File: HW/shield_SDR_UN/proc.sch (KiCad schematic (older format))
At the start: 53 parts

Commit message: bus-v2 proc-fpga
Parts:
- removed R? (x15): 39, symbol Device:R
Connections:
- net +5V is gone; now on net 3V3 MCU: J?.19 (Pin_19)
- net ADD_DAT_15 is gone; now on net GPIO_MCU_1: U?.10 ((PF0)(I2C2_SDA)(FMC_A0)(EVENTOUT))
- net ADD_DAT_16 is gone; now on net GPIO_MCU_2: U?.11 ((PF1)(I2C2_SCL)(FMC_A1)(EVENTOUT))
- net ADD_DAT_17 is gone; now on net GPIO_MCU_3: U?.12 ((PF2)(I2C2_SMBA)(FMC_A2)(EVENTOUT))
- net ADD_DAT_18 is gone; now on net GPIO_MCU_4: U?.13 ((PF3)(FMC_A3)(EVENTOUT)(ADC3_IN9))
- net ADD_DAT_19 is gone; now on net GPIO_MCU_5: U?.14 ((PF4)(FMC_A4)(EVENTOUT)(ADC3_IN14))
- net ADD_DAT_20 is gone; now on net GPIO_MCU_6: U?.15 ((PF5)(FMC_A5)(EVENTOUT)(ADC3_IN15))
- net ADD_DAT_21 is gone; now on net GPIO_MCU_7: U?.18 ((PF6)(TIM10_CH1)(SPI5_NSS)(SAI1_SD_B)(UART7_RX)(QUADSPI_BK1_IO3)(EVENTOUT)(ADC3_IN4))
- net ADD_DAT_22 is gone; now on net GPIO_MCU_8: U?.19 ((PF7)(TIM11_CH1)(SPI5_SCK)(SAI1_MCLK_B)(UART7_TX)(QUADSPI_BK1_IO2)(EVENTOUT)(ADC3_IN5))
- net ADD_DAT_23 is gone; now on net GPIO_MCU_9: U?.20 ((PF8)(SPI5_MISO)(SAI1_SCK_B)(UART7_RTS)(TIM13_CH1)(QUADSPI_BK1_IO0)(EVENTOUT)(ADC3_IN6))
- net ADD_DAT_24 is gone; now on net GPIO_MCU_10: U?.21 ((PF9)(SPI5_MOSI)(SAI1_FS_B)(UART7_CTS)(TIM14_CH1)(QUADSPI_BK1_IO1)(EVENTOUT)(ADC3_IN7))
- net ADD_DAT_25 is gone; now on net GPIO_MCU_11: U?.22 ((PF10)(EVENTOUT)(ADC3_IN8))
- net GPIO_MCU_1: no longer U?.141 ((PE0)(TIM4_ETR)(LPTIM1_ETR)(UART8_Rx)(SAI2_MCK_A)(FMC_NBL0)(EVENTOUT))
- net GPIO_MCU_10: no longer U?.60 ((PE9)(TIM1_CH1)(UART7_RTS)(QUADSPI_BK2_IO2)(FMC_D6)(EVENTOUT))
- net GPIO_MCU_11: no longer U?.63 ((PE10)(TIM1_CH2N)(UART7_CTS)(QUADSPI_BK2_IO3)(FMC_D7)(EVENTOUT))
- net GPIO_MCU_12: now also U?.26 ((SAI2_FS_B)(OTG_HS_ULPI_STP)(FMC_SDNWE)(EVENTOUT)(ADC1_IN10)(ADC2_IN10)(ADC3_IN10)(PC0)); no longer U?.64 ((PE11)(TIM1_CH2)(SPI4_NSS)(SAI2_SD_B)(FMC_D8)(EVENTOUT))
- net GPIO_MCU_13: now also U?.27 ((TRACED0)(SPI2_MOSI/I2S2_SD)(SAI1_SD_A)(EVENTOUT)(ADC1_IN11)(ADC2_IN11)(ADC3_IN11)(RTC_TAMP3)(WKUP3)(PC1)); no longer U?.65 ((PE12)(TIM1_CH3N)(SPI4_SCK)(SAI2_SCK_B)(FMC_D9)(EVENTOUT))
- net GPIO_MCU_14: now also U?.28 ((SPI2_MISO)(OTG_HS_ULPI_DIR)(FMC_SDNE0)(EVENTOUT)(ADC1_IN12)(ADC2_IN12)(ADC3_IN12)(PC2)); no longer U?.66 ((PE13)(TIM1_CH3)(SPI4_MISO)(SAI2_FS_B)(FMC_D10)(EVENTOUT))
- net GPIO_MCU_15: now also U?.29 ((SPI2_MOSI/I2S2_SD)(OTG_HS_ULPI_NXT)(FMC_SDCKE0)(EVENTOUT)(ADC1_IN13)(ADC2_IN13)(ADC3_IN13)(PC3)); no longer U?.67 ((PE14)(TIM1_CH4)(SPI4_MOSI)(SAI2_MCK_B)(FMC_D11)(EVENTOUT))
- net GPIO_MCU_16: now also U?.136 ((TIM4_CH1)(I2C1_SCL)(USART1_TX)(QUAD_SPI_BK1_NCS)(FMC_SDNE1)(EVENTOUT)(PB6)); no longer U?.68 ((PE15)(TIM1_BKIN)(FMC_D12)(EVENTOUT))
- net GPIO_MCU_2: no longer U?.142 ((PE1)(LPTIM1_IN2)(UART8_Tx)(FMC_NBL1)(EVENTOUT))
- net GPIO_MCU_3: no longer U?.1 ((PE2)(TRACECLK)(SPI4_SCK)(SAI1_MCLK_A)(QUADSPI_BK1_IO2)(FMC_A23)(EVENTOUT))
- net GPIO_MCU_4: no longer U?.2 ((PE3)(TRACED0)(SAI1_SD_B)(FMC_A19)(EVENTOUT))
- net GPIO_MCU_5: no longer U?.3 ((PE4)(TRACED1)(SPI4_NSS)(SAI1_FS_A)(FMC_A20)(EVENTOUT))
- net GPIO_MCU_6: no longer U?.4 ((PE5)(TRACED2)(TIM9_CH1)(SPI4_MISO)(SAI1_SCK_A)(FMC_A21)(EVENTOUT))
- net GPIO_MCU_7: no longer U?.5 ((PE6)(TRACED3)(TIM1_BKIN2)(TIM9_CH2)(SPI4_MOSI)(SAI1_SD_A)(SAI2_MCK_B)(FMC_A22)(EVENTOUT))
- net GPIO_MCU_8: no longer U?.58 ((PE7)(TIM1_ETR)(UART7_Rx)(QUADSPI_BK2_IO0)(FMC_D4)(EVENTOUT))
- net GPIO_MCU_9: no longer U?.59 ((PE8)(TIM1_CH1N)(UART7_Tx)(QUADSPI_BK2_IO1)(FMC_D5)(EVENTOUT))
- net FMC_NL: now reaches U?.137 ((TIM4_CH2)(I2C1_SDA)(USART1_RX)(FMC_NL)(EVENTOUT)(PB7))
- net I2C1_SCL: now reaches U?.139 ((TIM4_CH3)(TIM10_CH1)(I2C1_SCL)(CAN1_RX)(SDMMC2_D4)(SDMMC1_D4)(EVENTOUT)(PB8))
- net I2C1_SDA: now reaches U?.140 ((TIM4_CH4)(TIM11_CH1)(I2C1_SDA)(SPI2_NSS/I2S2_WS)(CAN1_TX)(SDMMC2_D5)(SDMMC1_D5)(EVENTOUT)(PB9))
- net FMC_D13: now reaches U?.77 ((USART3_TX)(FMC_D13)(EVENTOUT)(PD8))
- net FMC_D14: now reaches U?.78 ((USART3_RX)(FMC_D14)(EVENTOUT)(PD9))
- net FMC_D15: now reaches U?.79 ((USART3_CK)(FMC_D15)(EVENTOUT)(PD10))
- net FMC_A16: now reaches U?.80 ((USART3_CTS)(QUADSPI_BK1_IO0)(SAI2_SD_A)(FMC_A16/FMC_CLE)(EVENTOUT)(PD11))
- net FMC_A17: now reaches U?.81 ((TIM4_CH1)(LPTIM1_IN1)(USART3_RTS)(QUADSPI_BK1_IO1)(SAI2_FS_A)(FMC_A17/FMC_ALE)(EVENTOUT)(PD12))
- net FMC_A18: now reaches U?.82 ((TIM4_CH2)(LPTIM1_OUT)(QUADSPI_BK1_IO3)(SAI2_SCK_A)(FMC_A18)(EVENTOUT)(PD13))
- net FMC_D0: now reaches U?.85 ((TIM4_CH3)(UART8_CTS)(FMC_D0)(EVENTOUT)(PD14))
- net FMC_D1: now reaches U?.86 ((TIM4_CH4)(UART8_RTS)(FMC_D1)(EVENTOUT)(PD15))
- net FMC_A14: now reaches U?.89 ((PG4)(FMC_A14/FMC_BA0)(EVENTOUT))
- net FMC_A15: now reaches U?.90 ((PG5)(FMC_A15/FMC_BA1)(EVENTOUT))
- net ADD_DAT_26: no longer names the net of U?.49 ((PF11)(SPI5_MOSI)(SAI2_SD_B)(FMC_SDNRAS)(EVENTOUT))
- net ADD_DAT_27: no longer names the net of U?.50 ((PF12)(FMC_A6)(EVENTOUT))
- net ADD_DAT_28: no longer names the net of U?.53 ((PF13)(FMC_A7)(EVENTOUT))
- net ADD_DAT_29: no longer names the net of U?.54 ((PF14)(FMC_A8)(EVENTOUT))
- net ADD_DAT_30: no longer names the net of U?.55 ((PF15)(FMC_A9)(EVENTOUT))
- net P_FPGA_1: no longer names the net of U?.113 ((TRACED3)(SPI3_MOSI/I2S3_SD)(USART3_CK)(UART5_TX)(SDMMC1_CK)(EVENTOUT)(PC12))
- net P_FPGA_10: no longer names the net of U?.124 ((USART6_RX)(QUADSPI_BK2_IO2)(SAI2_FS_B)(SDMMC2_D0)(FMC_NE2/FMC_NCE)(EVENTOUT)(PG9))
- net P_FPGA_11: no longer names the net of U?.125 ((PG10)(SAI2_SD_B)(SDMMC2_D1)(FMC_NE3)(EVENTOUT))
- net P_FPGA_12: no longer names the net of U?.126 ((PG11)(SDMMC2_D2)(FMC_INT)(EVENTOUT))
- net P_FPGA_13: no longer names the net of U?.127 ((PG12)(LPTIM1_IN1)(USART6_RTS)(SDMMC2_D3)(FMC_NE4)(EVENTOUT))
- net P_FPGA_14: no longer names the net of U?.128 ((PG13)(TRACED0)(LPTIM1_OUT)(USART6_CTS)(FMC_A24)(EVENTOUT))
- net P_FPGA_15: no longer names the net of U?.129 ((PG14)(TRACED1)(LPTIM1_ETR)(USART6_TX)(QUADSPI_BK2_IO3)(FMC_A25)(EVENTOUT))
- net P_FPGA_2 renamed FMC_D2
- net P_FPGA_3 renamed FMC_D3
- net P_FPGA_4: no longer names the net of U?.116 ((TRACED2)(TIM3_ETR)(UART5_RX)(SDMMC1_CMD)(EVENTOUT)(PD2))
- net P_FPGA_5 renamed FMC_CLK
- net P_FPGA_6 renamed FMC_NOE
- net P_FPGA_7 renamed FMC_NWE
- net P_FPGA_8 renamed FMC_NWAIT
- net P_FPGA_9 renamed FMC_NE1
- new net FMC_A19: U?.2 ((PE3)(TRACED0)(SAI1_SD_B)(FMC_A19)(EVENTOUT))
- new net FMC_A20: U?.3 ((PE4)(TRACED1)(SPI4_NSS)(SAI1_FS_A)(FMC_A20)(EVENTOUT))
- new net FMC_A21: U?.4 ((PE5)(TRACED2)(TIM9_CH1)(SPI4_MISO)(SAI1_SCK_A)(FMC_A21)(EVENTOUT))
- new net FMC_A22: U?.5 ((PE6)(TRACED3)(TIM1_BKIN2)(TIM9_CH2)(SPI4_MOSI)(SAI1_SD_A)(SAI2_MCK_B)(FMC_A22)(EVENTOUT))
- new net FMC_A23: U?.1 ((PE2)(TRACECLK)(SPI4_SCK)(SAI1_MCLK_A)(QUADSPI_BK1_IO2)(FMC_A23)(EVENTOUT))
- new net FMC_D10: U?.66 ((PE13)(TIM1_CH3)(SPI4_MISO)(SAI2_FS_B)(FMC_D10)(EVENTOUT))
- new net FMC_D11: U?.67 ((PE14)(TIM1_CH4)(SPI4_MOSI)(SAI2_MCK_B)(FMC_D11)(EVENTOUT))
- new net FMC_D12: U?.68 ((PE15)(TIM1_BKIN)(FMC_D12)(EVENTOUT))
- new net FMC_D4: U?.58 ((PE7)(TIM1_ETR)(UART7_Rx)(QUADSPI_BK2_IO0)(FMC_D4)(EVENTOUT))
- new net FMC_D5: U?.59 ((PE8)(TIM1_CH1N)(UART7_Tx)(QUADSPI_BK2_IO1)(FMC_D5)(EVENTOUT))
- new net FMC_D6: U?.60 ((PE9)(TIM1_CH1)(UART7_RTS)(QUADSPI_BK2_IO2)(FMC_D6)(EVENTOUT))
- new net FMC_D7: U?.63 ((PE10)(TIM1_CH2N)(UART7_CTS)(QUADSPI_BK2_IO3)(FMC_D7)(EVENTOUT))
- new net FMC_D8: U?.64 ((PE11)(TIM1_CH2)(SPI4_NSS)(SAI2_SD_B)(FMC_D8)(EVENTOUT))
- new net FMC_D9: U?.65 ((PE12)(TIM1_CH3N)(SPI4_SCK)(SAI2_SCK_B)(FMC_D9)(EVENTOUT))
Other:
- note added: "BUS DATA-ADDRESS-CONTROL \nPROC<->FPGA\n"
- note added: "FMC_NADV o NL\n"

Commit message: algunos footprint
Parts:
- added L? (x2): bead, 600R, 350 mA, Inductor_SMD:L_0603_1608Metric_Pad1.05x0.95mm_HandSolder, symbol Device:L
- added Y?: ABM8G-25.000MHZ-B4Y-T, UL_ABM9G25000MHZB4YT:ABM8G-25.000MHZ-B4Y-T, symbol UL_ABM9G25000MHZB4YT:ABM8G-25.000MHZ-B4Y-T
- BT?: footprint (none) -> modules:BAT-HLD-001; digikey (none) -> BAT-HLD-001-ND
- C? (x4): footprint (none) -> Capacitor_SMD:C_0603_1608Metric_Pad1.05x0.95mm_HandSolder
- D? (x2): footprint (none) -> LED_SMD:LED_0805_2012Metric_Pad1.15x1.40mm_HandSolder
- J?: footprint (none) -> Connector_PinSocket_2.54mm:PinSocket_2x20_P2.54mm_Vertical; DIGIKEY (none) -> S6106-ND
- R? (x4): footprint (none) -> Resistor_SMD:R_0603_1608Metric_Pad1.05x0.95mm_HandSolder
- U?: footprint (none) -> Package_QFP:LQFP-144_20x20mm_P0.5mm; digikey (none) -> 497-18558-ND
- X?: footprint (none) -> CRISTAL_4:GSG-XTAL3.2x2.5mm; digikey 535-10297-1-ND////535-11296-1-ND -> 535-10289-1-ND
- X?: footprint (none) -> CRISTAL_4:NX3215SA; digikey SER4103CT-ND -> 644-1171-1-ND
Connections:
- wire segments 328 -> 329
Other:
- note added: "587-1897-1-ND"

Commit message: algunos footprint_v2
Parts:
- removed X?: GSG-XTAL4PIN, CRISTAL_4:GSG-XTAL3.2x2.5mm, symbol hackrf-one-rescue:GSG-XTAL4PIN
- removed Y?: ABM8G-25.000MHZ-B4Y-T, UL_ABM9G25000MHZB4YT:ABM8G-25.000MHZ-B4Y-T, symbol UL_ABM9G25000MHZB4YT:ABM8G-25.000MHZ-B4Y-T
- added Y?e: GSG-XTAL4PIN, CRISTAL_4:GSG-XTAL3.2x2.5mm, symbol UL_ABM9G25000MHZB4YT:ABM8G-25.000MHZ-B4Y-T
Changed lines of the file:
@@
-$EndComp
-$Comp
-L hackrf-one-rescue:GSG-XTAL4PIN X?
-U 0 0 5CD3D0E7
-P 2100 4700
-F 0 "X?" H 2100 5083 60  0000 C CNN
-F 1 "GSG-XTAL4PIN" H 2100 4977 60  0000 C CNN
-F 2 "CRISTAL_4:GSG-XTAL3.2x2.5mm" H 2100 4700 60  0001 C CNN
-F 3 "" H 2100 4700 60  0000 C CNN
-F 4 "16MHz - 10pF" H 2100 4879 50  0000 C CNN "frecuencia"
-F 5 "	535-10289-1-ND" H 2100 4700 50  0001 C CNN "digikey"
-	0    2100 4700
-	1    0    0    -1
 $EndComp
 $Comp
 L power:GND #PWR0164
 U 1 1 5CD657FB
-P 2000 5100
-F 0 "#PWR0164" H 2000 4850 50  0001 C CNN
-F 1 "GND" H 2005 4927 50  0000 C CNN
-F 2 "" H 2000 5100 50  0001 C CNN
-F 3 "" H 2000 5100 50  0001 C CNN
-	1    2000 5100
-	1    0    0    -1
+P 2050 4500
+F 0 "#PWR0164" H 2050 4250 50  0001 C CNN
+F 1 "GND" H 2055 4327 50  0000 C CNN
+F 2 "" H 2050 4500 50  0001 C CNN
+F 3 "" H 2050 4500 50  0001 C CNN
+	1    2050 4500
+	0    1    1    0
 $EndComp
 $Comp
 L power:GND #PWR0165
 U 1 1 5CD65D12
-P 2200 5100
-F 0 "#PWR0165" H 2200 4850 50  0001 C CNN
-F 1 "GND" H 2205 4927 50  0000 C CNN
-F 2 "" H 2200 5100 50  0001 C CNN
-F 3 "" H 2200 5100 50  0001 C CNN
-	1    2200 5100
-	1    0    0    -1
-$EndComp
-Wire Wire Line
-	2000 5100 2000 5000
-Wire Wire Line
-	2200 5100 2200 5000
+P 2150 5000
+F 0 "#PWR0165" H 2150 4750 50  0001 C CNN
+F 1 "GND" H 2155 4827 50  0000 C CNN
+F 2 "" H 2150 5000 50  0001 C CNN
+F 3 "" H 2150 5000 50  0001 C CNN
+	1    2150 5000
+	1    0    0    -1
+$EndComp
+Wire Wire Line
+	2050 4500 2150 4500
+Wire Wire Line
+	2150 5000 2150 4900
 $Comp
 L Device:C C?
@@
 Wire Wire Line
 	2750 4700 2400 4700
-Wire Wire Line
-	1800 4700 1450 4700
 Wire Wire Line
 	1450 4700 1450 4800
@@
 $Comp
 L hackrf-one-rescue:CRYSTAL X?
-U 0 0 5CDEC498
+U 1 1 5CDEC498
 P 2100 6200
 F 0 "X?" H 2100 6582 60  0000 C CNN
@@
 F 4 "32.768KHz -- 6pF" H 2100 6378 50  0000 C CNN "frecuencia"
 F 5 "644-1171-1-ND" H 2100 6200 50  0001 C CNN "digikey"
-	0    2100 6200
+	1    2100 6200
 	1    0    0    -1
 $EndComp
@@
 $Comp
 L Device:R R?
-U 0 0 5CD462E5
+U 1 1 5CD462E5
 P 1350 9800
 F 0 "R?" V 1450 9800 50  0000 L CNN
@@
 F 2 "Resistor_SMD:R_0603_1608Metric_Pad1.05x0.95mm_HandSolder" V 1280 9800 50  0001 C CNN
 F 3 "~" H 1350 9800 50  0001 C CNN
-	0    1350 9800
+	1    1350 9800
 	0    -1   -1   0
 $EndComp
@@
 $Comp
 L Device:LED D?
-U 0 0 5CE7E335
+U 1 1 5CE7E335
 P 16550 2000
 F 0 "D?" V 16589 1883 50  0000 R CNN
@@
 F 2 "LED_SMD:LED_0805_2012Metric_Pad1.15x1.40mm_HandSolder" H 16550 2000 50  0001 C CNN
 F 3 "~" H 16550 2000 50  0001 C CNN
-	0    16550 2000
+	1    16550 2000
 	0    -1   -1   0
 $EndComp
 $Comp
 L Device:LED D?
-U 0 0 5CE83502
+U 1 1 5CE83502
 P 17400 2000
 F 0 "D?" V 17439 1883 50  0000 R CNN
@@
 F 2 "LED_SMD:LED_0805_2012Metric_Pad1.15x1.40mm_HandSolder" H 17400 2000 50  0001 C CNN
 F 3 "~" H 17400 2000 50  0001 C CNN
-	0    17400 2000
+	1    17400 2000
 	0    -1   -1   0
 $EndComp
@@
 $Comp
 L Connector_Generic:Conn_02x10_Top_Bottom J?
-U 0 0 5D1F8415
+U 1 1 5D1F8415
 P 2450 12450
 F 0 "J?" H 2500 13067 50  0000 C CNN
@@
 F 3 "~" H 2450 12450 50  0001 C CNN
 F 4 "S6106-ND" H 2450 12450 50  0001 C CNN "DIGIKEY"
-	0    2450 12450
+	1    2450 12450
 	1    0    0    -1
 $EndComp
@@
 587-1897-1-ND
 $Comp
-L UL_ABM9G25000MHZB4YT:ABM8G-25.000MHZ-B4Y-T Y?
-U 0 0 5DF14116
-P 3500 5250
-F 0 "Y?" H 3944 5303 60  0000 L CNN
-F 1 "ABM8G-25.000MHZ-B4Y-T" H 3944 5197 60  0000 L CNN
-F 2 "UL_ABM9G25000MHZB4YT:ABM8G-25.000MHZ-B4Y-T" H 3700 4890 60  0001 C CNN
-F 3 "" H 3500 5250 60  0000 C CNN
-	0    3500 5250
-	1    0    0    -1
-$EndComp
+L UL_ABM9G25000MHZB4YT:ABM8G-25.000MHZ-B4Y-T Y?e
+U 0 0 5D0A0635
+P 1950 4700
+F 0 "Y?e" H 2300 5050 60  0000 L CNN
+F 1 "GSG-XTAL4PIN" H 2300 4950 60  0000 L CNN
+F 2 "CRISTAL_4:GSG-XTAL3.2x2.5mm" H 2150 4340 60  0001 C CNN
+F 3 "" H 1950 4700 60  0000 C CNN
+F 4 "16MHz - 10pF" H 2600 4850 50  0000 C CNN "frecuencia"
+F 5 "535-10289-1-ND" H 1950 4700 50  0001 C CNN "digikey"
+	0    1950 4700
+	1    0    0    -1
+$EndComp
+Wire Wire Line
+	1450 4700 1950 4700
 Wire Bus Line
 	7850 12700 7850 12900

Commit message: RF-Frontend balun
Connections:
- net GND: now also Y?e.2 (GND), Y?e.4 (GND)
- net OSC_IN: now also Y?e.1
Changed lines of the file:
@@
 $Comp
 L UL_ABM9G25000MHZB4YT:ABM8G-25.000MHZ-B4Y-T Y?e
-U 0 0 5D0A0635
+U 1 1 5D0A0635
 P 1950 4700
 F 0 "Y?e" H 2300 5050 60  0000 L CNN
@@
 F 4 "16MHz - 10pF" H 2600 4850 50  0000 C CNN "frecuencia"
 F 5 "535-10289-1-ND" H 1950 4700 50  0001 C CNN "digikey"
-	0    1950 4700
+	1    1950 4700
 	1    0    0    -1
 $EndComp

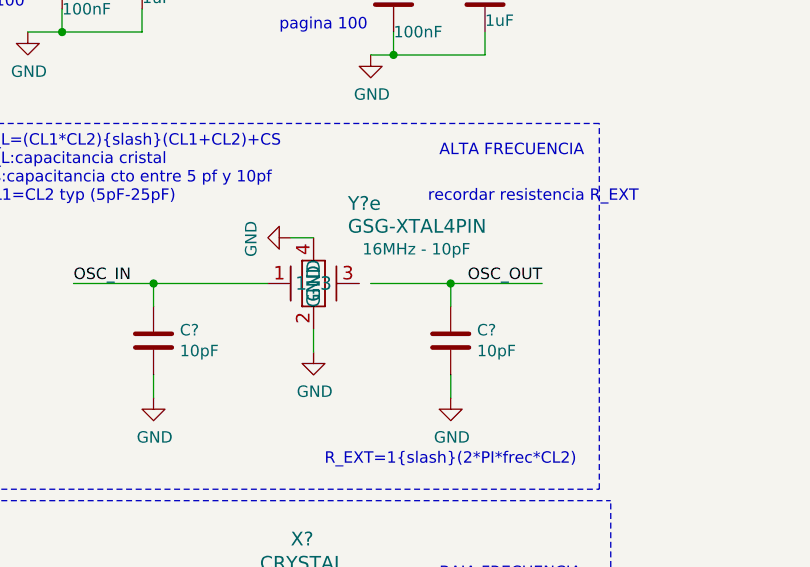
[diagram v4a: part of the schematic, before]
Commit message: se agrego el chip multirelojes
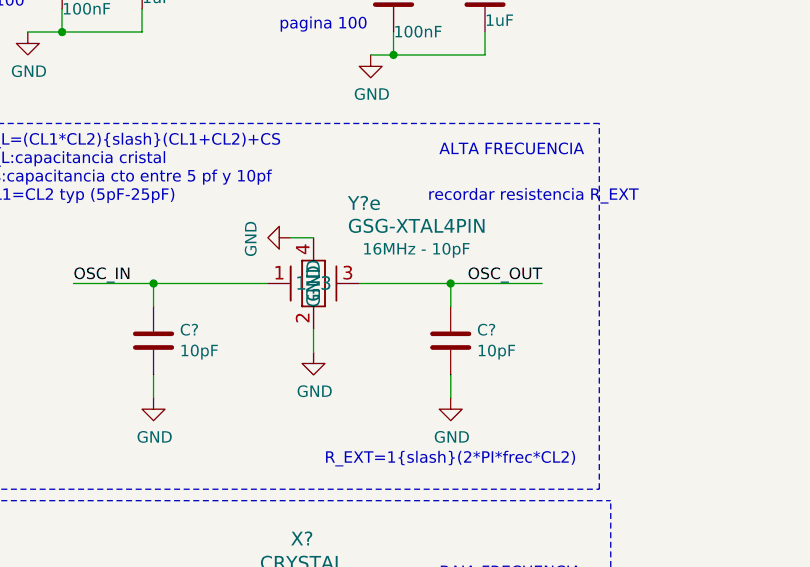
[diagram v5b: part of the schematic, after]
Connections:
- net OSC_OUT: now also Y?e.3
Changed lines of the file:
@@
 	2750 4800 2750 4700
-Wire Wire Line
-	2750 4700 2400 4700
 Wire Wire Line
 	1450 4700 1450 4800
@@
 Wire Wire Line
 	1450 4700 1950 4700
+Wire Wire Line
+	2350 4700 2750 4700
 Wire Bus Line
 	7850 12700 7850 12900

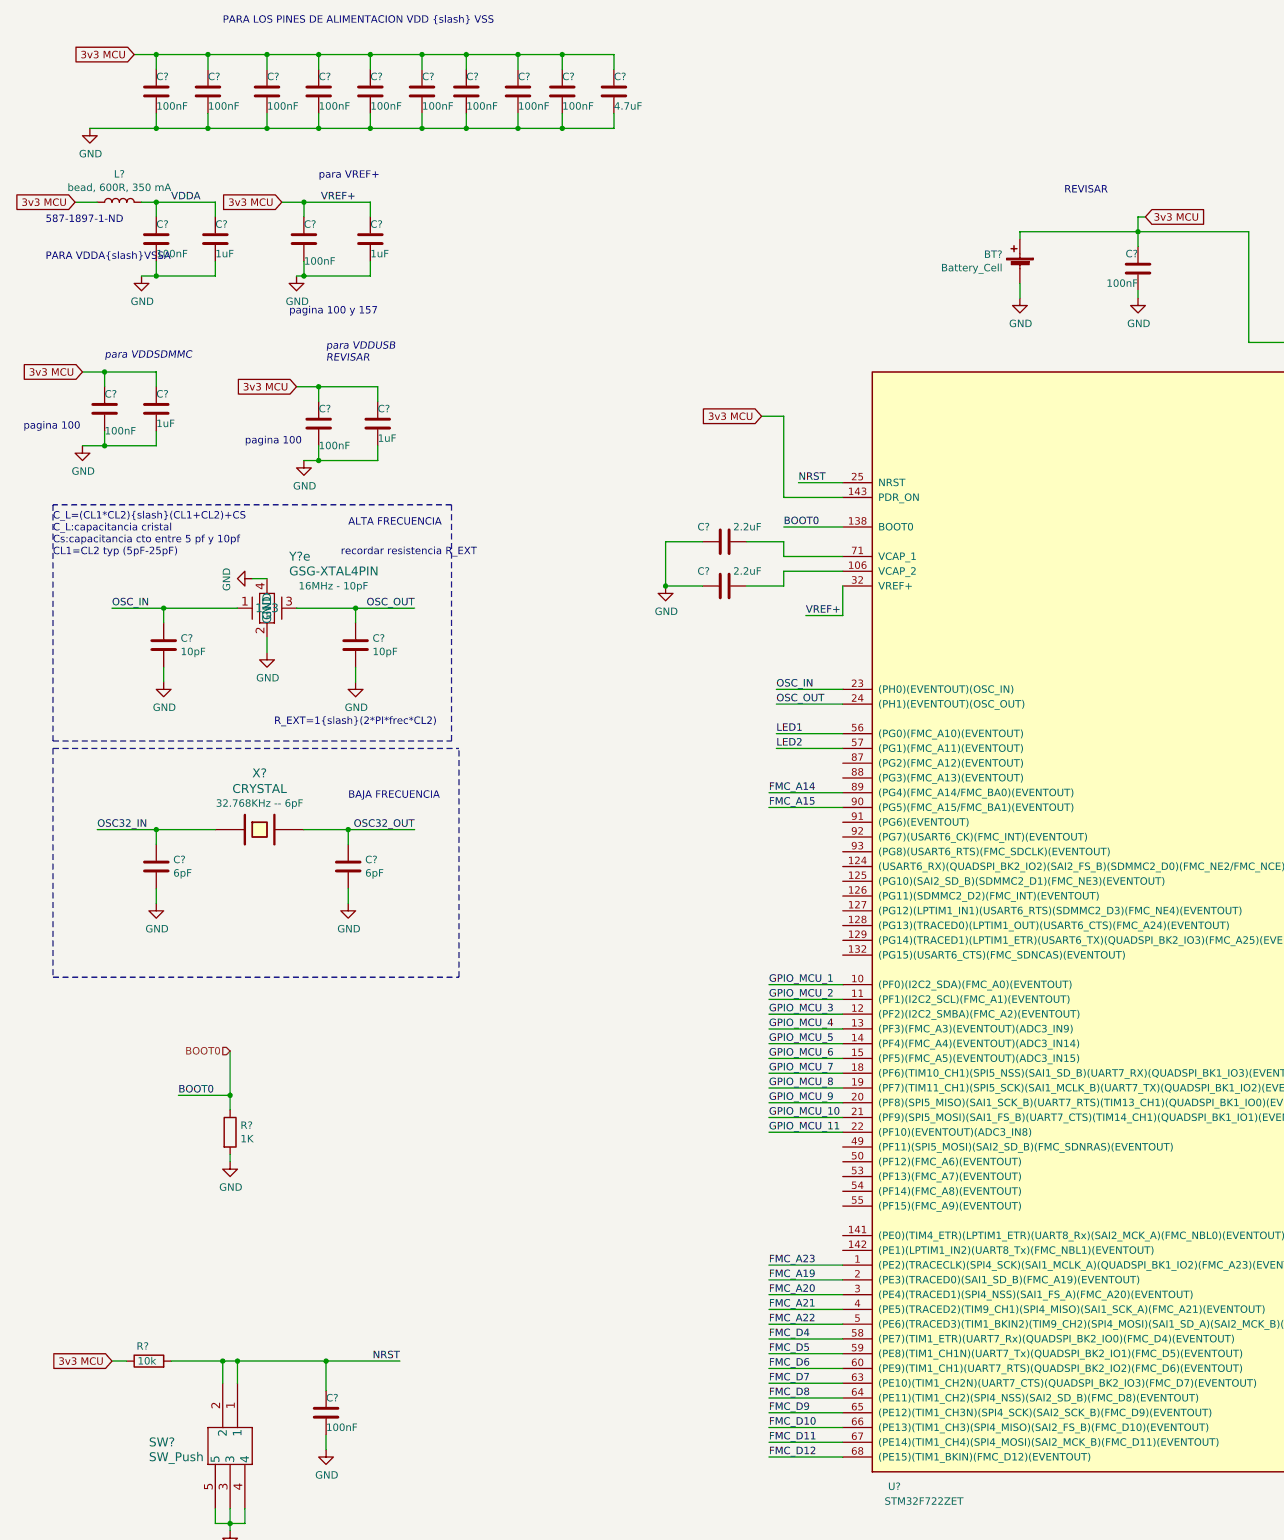
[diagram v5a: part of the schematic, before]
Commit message: Footprints added for C and R
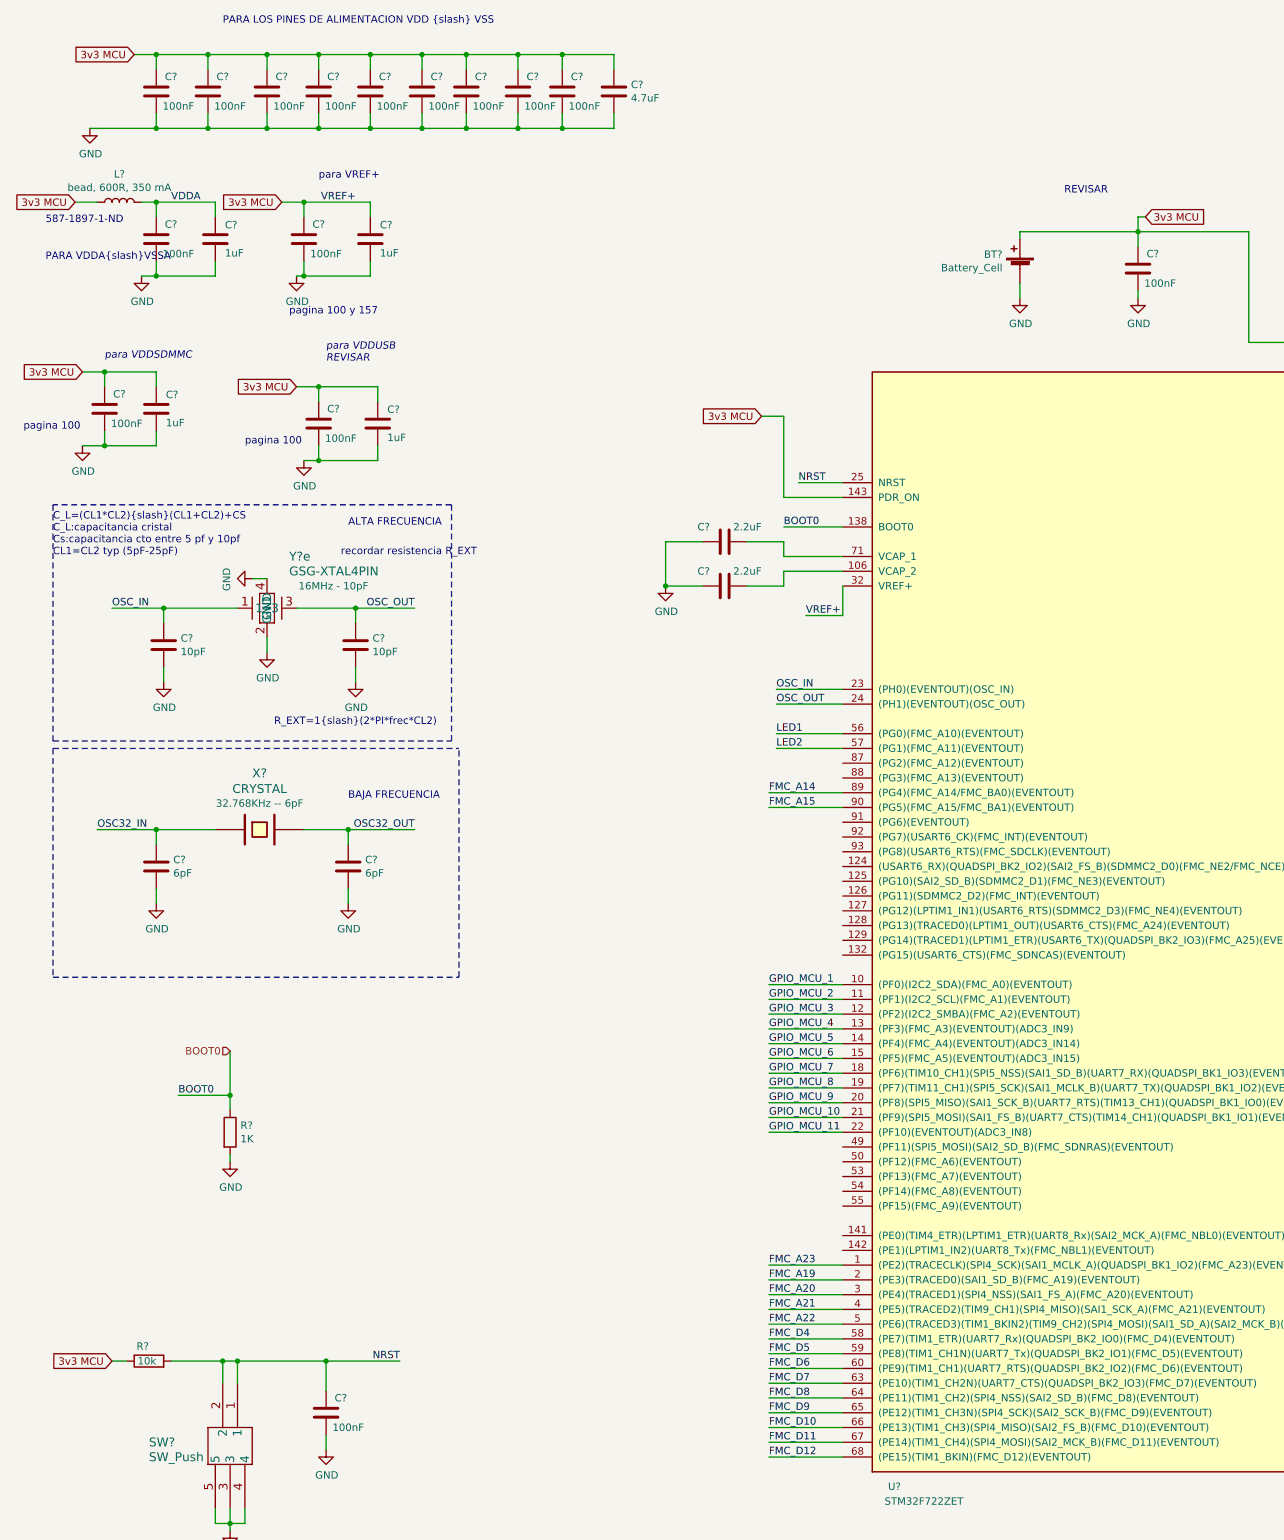
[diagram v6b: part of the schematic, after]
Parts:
- removed C? (x15): 100nF, Capacitor_SMD:C_0402_1005Metric, symbol Device:C
- removed C?: 4.7uF, Capacitor_SMD:C_0402_1005Metric, symbol Device:C
- removed C? (x4): 1uF, Capacitor_SMD:C_0402_1005Metric, symbol Device:C
- added C?: 4.7uF, Capacitor_SMD:C_0603_1608Metric_Pad1.05x0.95mm_HandSolder, symbol Device:C
- added C? (x15): 100nF, Capacitor_SMD:C_0603_1608Metric_Pad1.05x0.95mm_HandSolder, symbol Device:C
- added C? (x4): 1uF, Capacitor_SMD:C_0402_1005Metric, symbol Device:C
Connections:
- net 3v3 MCU: now also C?.1, C?.1, C?.1, C?.1, C?.1, C?.1, C?.1, C?.1, C?.1, C?.1, C?.1, C?.1, C?.1, C?.1, C?.1, C?.1, C?.1
- net GND: now also C?.2, C?.2, C?.2, C?.2, C?.2, C?.2, C?.2, C?.2, C?.2, C?.2, C?.2, C?.2, C?.2, C?.2, C?.2, C?.2, C?.2, C?.2, C?.2, C?.2
- net JTAG5: now also C?.1
- net VDDA: now also C?.1, C?.1
